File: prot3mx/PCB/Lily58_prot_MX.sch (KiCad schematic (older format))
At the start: 87 parts, among them J1 LED, J2 4PIN, J3 OLED, P1 i2c_pin, P2 i2c_pin, SW1 SW_PUSH, SW10 SW_PUSH, SW11 SW_PUSH, SW12 SW_PUSH, SW13 SW_PUSH, SW14 SW_PUSH, SW15 SW_PUSH, SW16 SW_PUSH, SW17 SW_PUSH, SW18 SW_PUSH, SW19 SW_PUSH, SW2 SW_PUSH, SW20 SW_PUSH, SW21 SW_PUSH, SW22 SW_PUSH, SW23 SW_PUSH, SW24 SW_PUSH, SW25 SW_PUSH, SW26 SW_PUSH, SW27 SW_PUSH, SW28 SW_PUSH, SW29 SW_PUSH, SW3 SW_PUSH, SW30 ROT_ENC_SW, SW31 ROT_ENC_SW, SW32 ROT_ENC_SW, SW4 SW_PUSH, SW5 SW_PUSH, SW6 SW_PUSH, SW7 SW_PUSH, SW8 SW_PUSH, SW9 SW_PUSH, U1 ProMicro

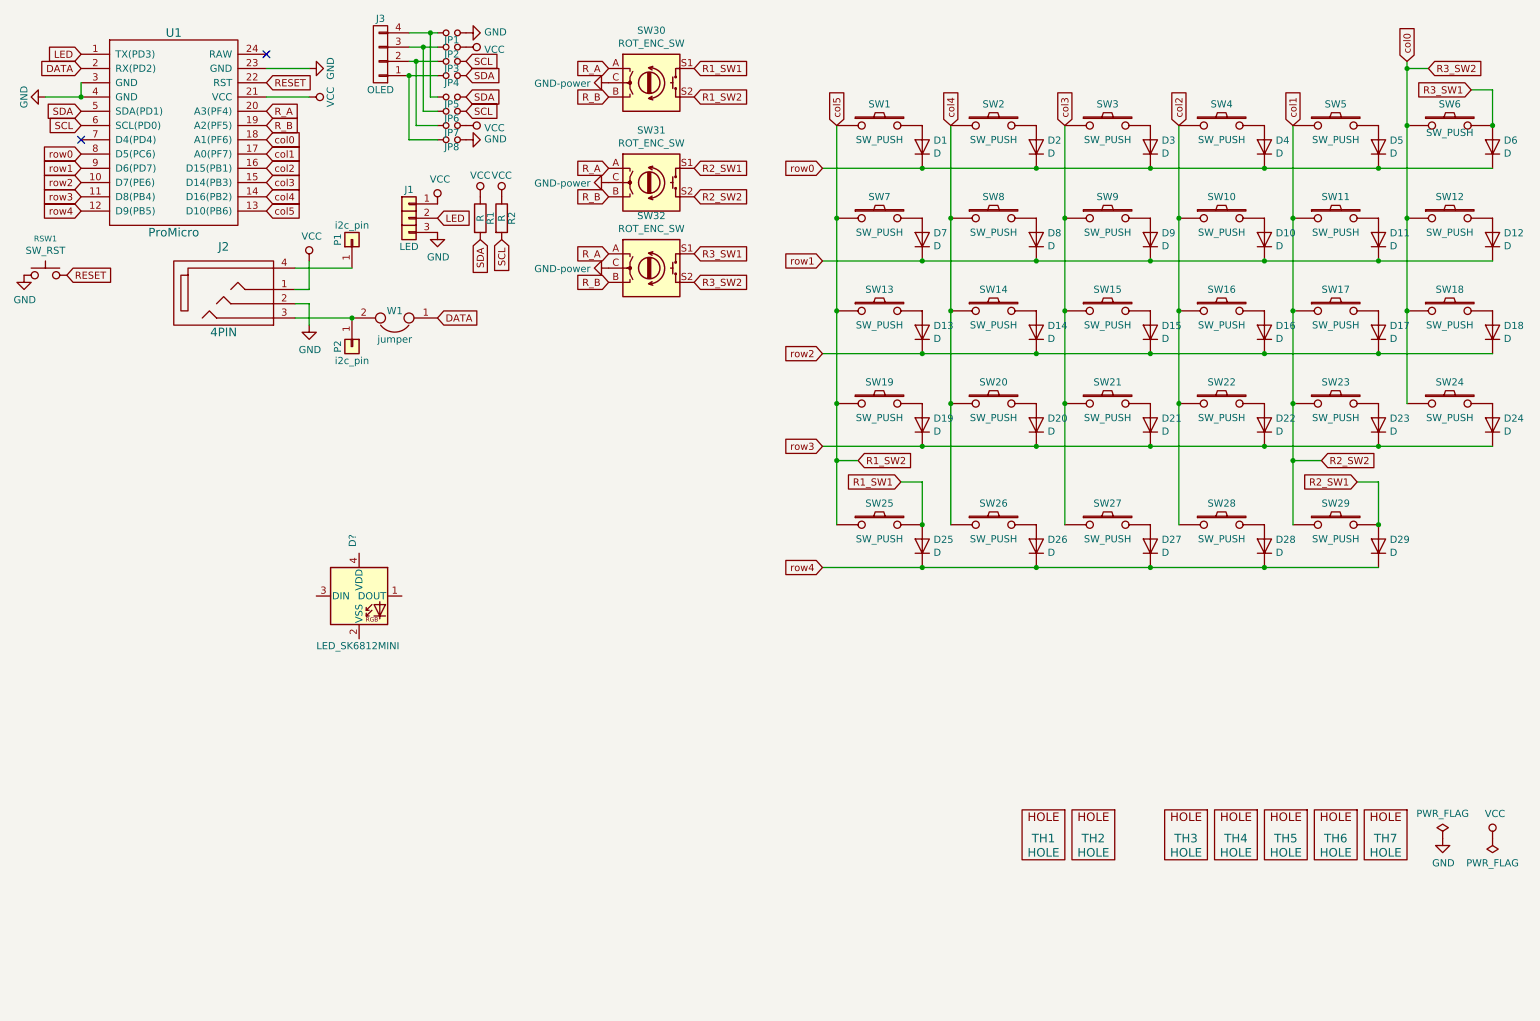
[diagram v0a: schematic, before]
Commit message: LEDs added to schematic; switch footprints flippped; tracks deleted; rerouting started
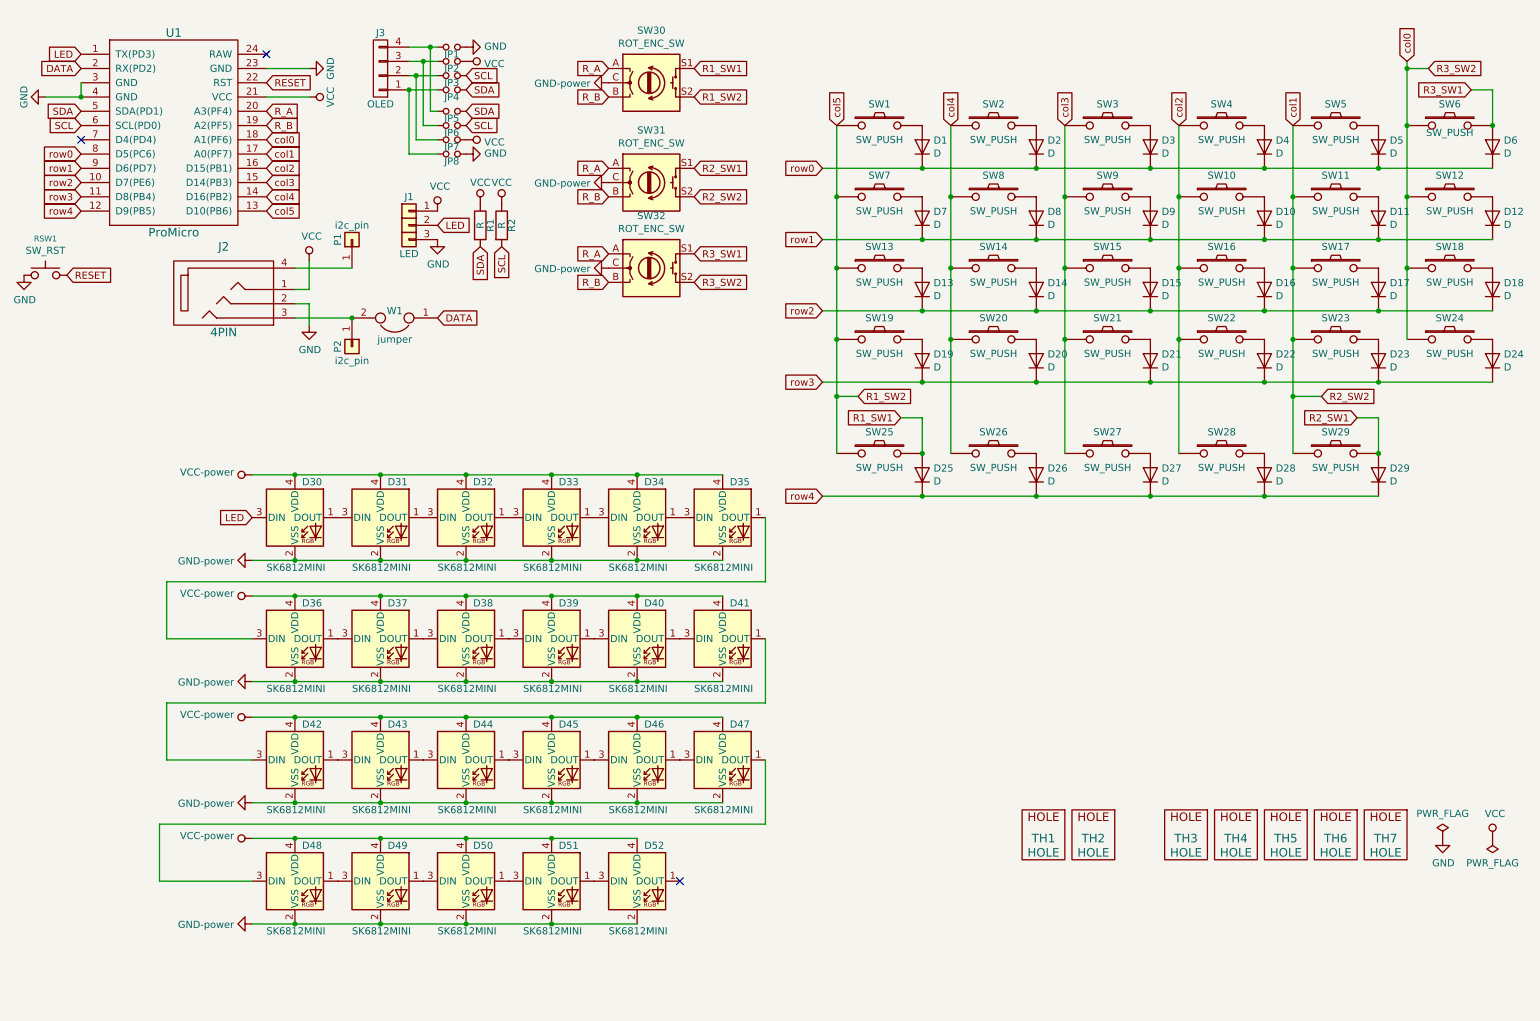
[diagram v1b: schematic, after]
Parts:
- added D31, D32, D33, D34, D35, D36, D37, D38, D39, D40, D41, D42, D43, D44, D45, D46, D47, D48, D49, D50, D51, D52: SK6812MINI, Lily58_prot_MX-footprint:SK6812MINI_rev, symbol Lily58_prot_MX-rescue:LED_SK6812MINI
- D30: renamed from D?; value LED_SK6812MINI -> SK6812MINI; footprint LED_SMD:LED_SK6812MINI_PLCC4_3.5x3.5mm_P1.75mm -> Lily58_prot_MX-footprint:SK6812MINI_rev
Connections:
- net GND: now also D30.2 (VSS), D31.2 (VSS), D32.2 (VSS), D33.2 (VSS), D34.2 (VSS), D35.2 (VSS), D36.2 (VSS), D37.2 (VSS), D38.2 (VSS), D39.2 (VSS), D40.2 (VSS), D41.2 (VSS), D42.2 (VSS), D43.2 (VSS), D44.2 (VSS), D45.2 (VSS), D46.2 (VSS), D47.2 (VSS), D48.2 (VSS), D49.2 (VSS), D50.2 (VSS), D51.2 (VSS), D52.2 (VSS)
- net LED: now also D30.3 (DIN)
- net VCC: now also D30.4 (VDD), D31.4 (VDD), D32.4 (VDD), D33.4 (VDD), D34.4 (VDD), D35.4 (VDD), D36.4 (VDD), D37.4 (VDD), D38.4 (VDD), D39.4 (VDD), D40.4 (VDD), D41.4 (VDD), D42.4 (VDD), D43.4 (VDD), D44.4 (VDD), D45.4 (VDD), D46.4 (VDD), D47.4 (VDD), D48.4 (VDD), D49.4 (VDD), D50.4 (VDD), D51.4 (VDD), D52.4 (VDD)
- net at D30.1 (DOUT): now also D31.3 (DIN)
- new net: D31.1 (DOUT), D32.3 (DIN)
- new net: D32.1 (DOUT), D33.3 (DIN)
- new net: D33.1 (DOUT), D34.3 (DIN)
- new net: D34.1 (DOUT), D35.3 (DIN)
- new net: D35.1 (DOUT), D36.3 (DIN)
- new net: D36.1 (DOUT), D37.3 (DIN)
- new net: D37.1 (DOUT), D38.3 (DIN)
- new net: D38.1 (DOUT), D39.3 (DIN)
- new net: D39.1 (DOUT), D40.3 (DIN)
- new net: D40.1 (DOUT), D41.3 (DIN)
- new net: D41.1 (DOUT), D42.3 (DIN)
- new net: D42.1 (DOUT), D43.3 (DIN)
- new net: D43.1 (DOUT), D44.3 (DIN)
- new net: D44.1 (DOUT), D45.3 (DIN)
- new net: D45.1 (DOUT), D46.3 (DIN)
- new net: D46.1 (DOUT), D47.3 (DIN)
- new net: D47.1 (DOUT), D48.3 (DIN)
- new net: D48.1 (DOUT), D49.3 (DIN)
- new net: D49.1 (DOUT), D50.3 (DIN)
- new net: D50.1 (DOUT), D51.3 (DIN)
- new net: D51.1 (DOUT), D52.3 (DIN)
- no-connect marks 2 -> 3
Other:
- moved on the sheet: D10, D11, D12, D13, D14, D15, D16, D17, D18, D19, D20, D21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

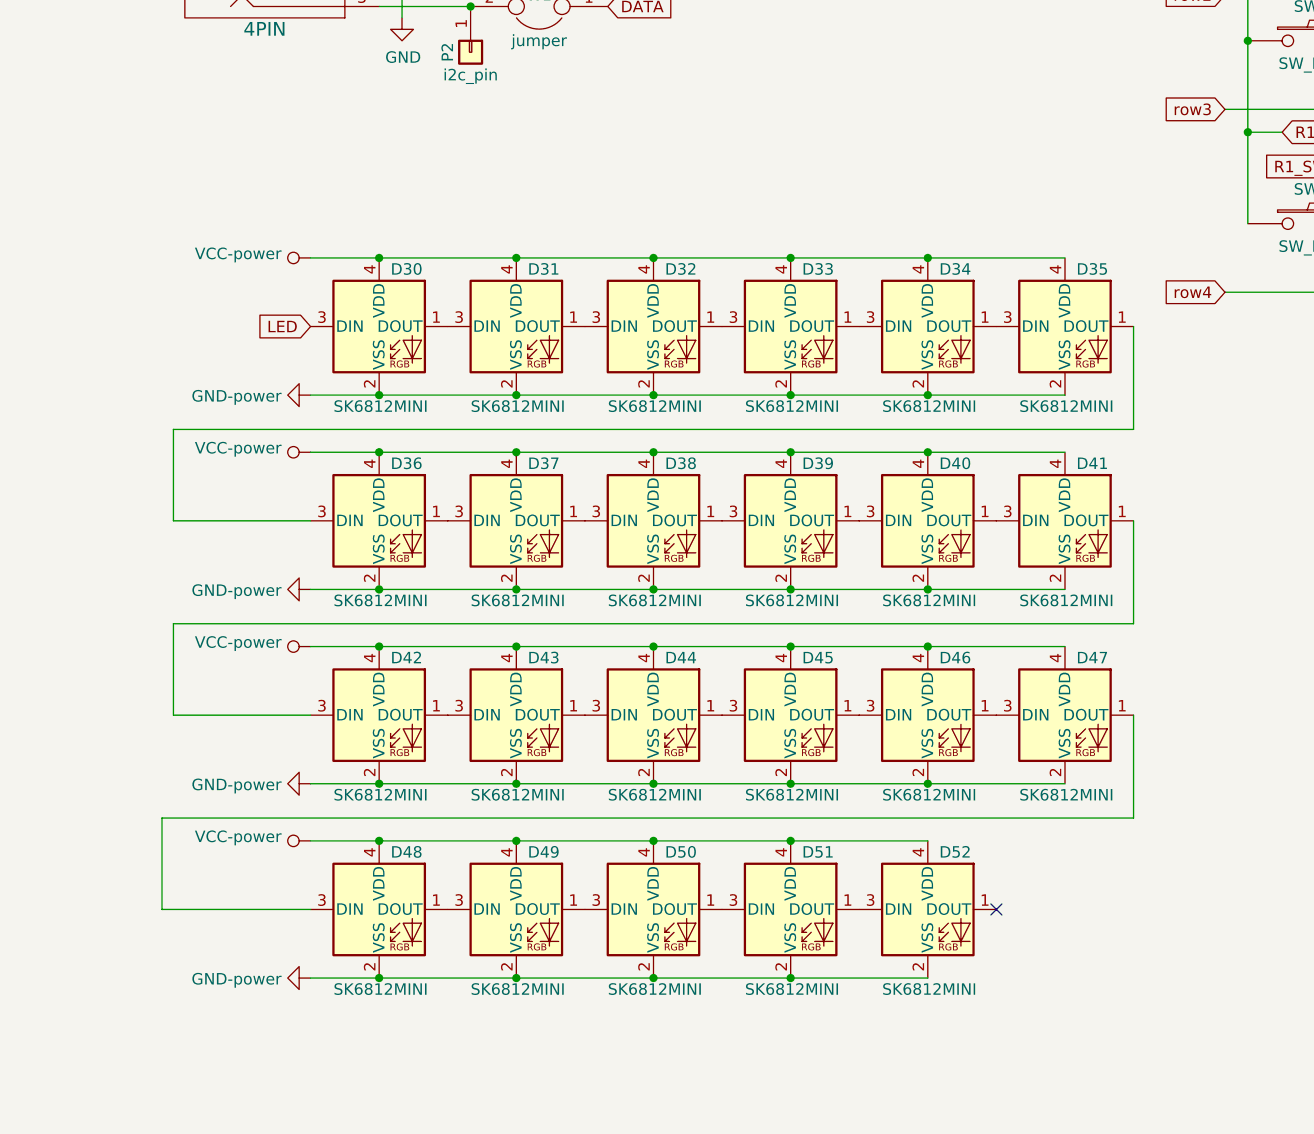
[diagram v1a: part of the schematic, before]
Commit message: modified SK6812 footprint to include cutout
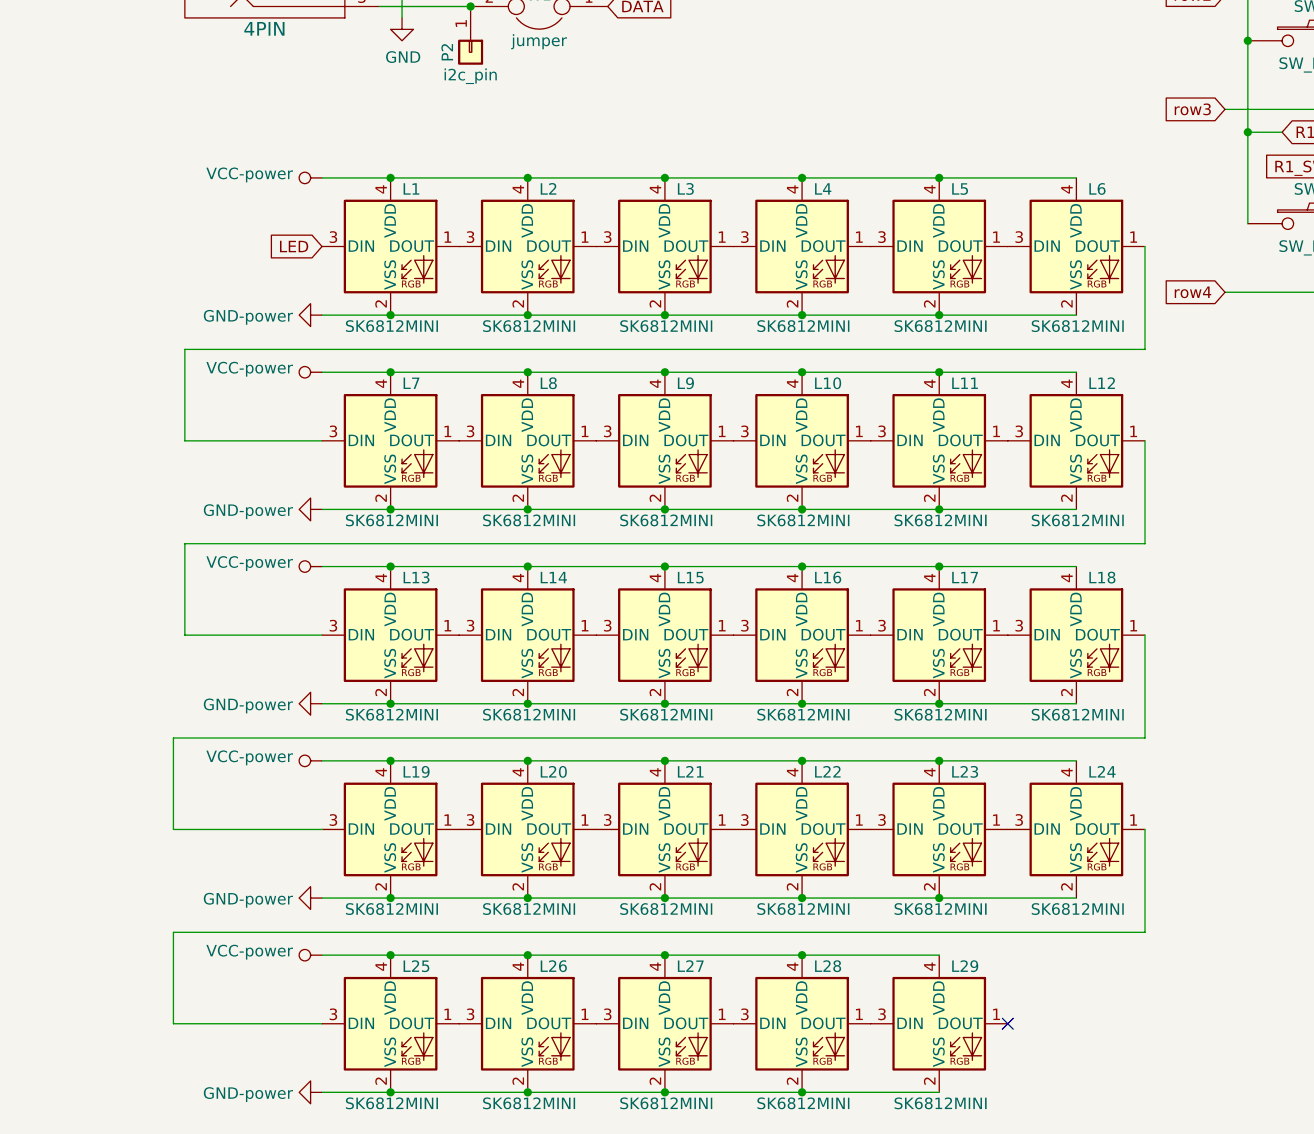
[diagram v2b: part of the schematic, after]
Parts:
- removed D31, D32, D33, D34, D35, D36, D37, D38, D39, D40, D41, D42, D43, D44, D45, D46, D47, D48, D49, D50, D51, D52: SK6812MINI, Lily58_prot_MX-footprint:SK6812MINI_rev, symbol Lily58_prot_MX-rescue:LED_SK6812MINI
- added L10, L11, L12, L13, L14, L15, L16, L17, L18, L19, L2, L20, L21, L22, L23, L24, L25, L26, L27, L28, L29, L3, L4, L5, L6, L7, L8, L9: SK6812MINI, Lily58_prot_MX-footprint:SK6812MINI_rev_w_co, symbol Lily58_prot_MX-rescue:LED_SK6812MINI
- L1: renamed from D30; footprint Lily58_prot_MX-footprint:SK6812MINI_rev -> Lily58_prot_MX-footprint:SK6812MINI_rev_w_co
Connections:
- net GND: now also L10.2 (VSS), L11.2 (VSS), L12.2 (VSS), L13.2 (VSS), L14.2 (VSS), L15.2 (VSS), L16.2 (VSS), L17.2 (VSS), L18.2 (VSS), L19.2 (VSS), L2.2 (VSS), L20.2 (VSS), L21.2 (VSS), L22.2 (VSS), L23.2 (VSS), L24.2 (VSS), L25.2 (VSS), L26.2 (VSS), L27.2 (VSS), L28.2 (VSS), L29.2 (VSS), L3.2 (VSS), L4.2 (VSS), L5.2 (VSS), L6.2 (VSS), L7.2 (VSS), L8.2 (VSS), L9.2 (VSS)
- net VCC: now also L10.4 (VDD), L11.4 (VDD), L12.4 (VDD), L13.4 (VDD), L14.4 (VDD), L15.4 (VDD), L16.4 (VDD), L17.4 (VDD), L18.4 (VDD), L19.4 (VDD), L2.4 (VDD), L20.4 (VDD), L21.4 (VDD), L22.4 (VDD), L23.4 (VDD), L24.4 (VDD), L25.4 (VDD), L26.4 (VDD), L27.4 (VDD), L28.4 (VDD), L29.4 (VDD), L3.4 (VDD), L4.4 (VDD), L5.4 (VDD), L6.4 (VDD), L7.4 (VDD), L8.4 (VDD), L9.4 (VDD)
- net at L1.1 (DOUT): now also L2.3 (DIN)
- new net: L2.1 (DOUT), L3.3 (DIN)
- new net: L3.1 (DOUT), L4.3 (DIN)
- new net: L4.1 (DOUT), L5.3 (DIN)
- new net: L5.1 (DOUT), L6.3 (DIN)
- new net: L6.1 (DOUT), L7.3 (DIN)
- new net: L7.1 (DOUT), L8.3 (DIN)
- new net: L8.1 (DOUT), L9.3 (DIN)
- new net: L10.3 (DIN), L9.1 (DOUT)
- new net: L10.1 (DOUT), L11.3 (DIN)
- new net: L11.1 (DOUT), L12.3 (DIN)
- new net: L12.1 (DOUT), L13.3 (DIN)
- new net: L13.1 (DOUT), L14.3 (DIN)
- new net: L14.1 (DOUT), L15.3 (DIN)
- new net: L15.1 (DOUT), L16.3 (DIN)
- new net: L16.1 (DOUT), L17.3 (DIN)
- new net: L17.1 (DOUT), L18.3 (DIN)
- new net: L18.1 (DOUT), L19.3 (DIN)
- new net: L19.1 (DOUT), L20.3 (DIN)
- new net: L20.1 (DOUT), L21.3 (DIN)
- new net: L21.1 (DOUT), L22.3 (DIN)
- new net: L22.1 (DOUT), L23.3 (DIN)
- new net: L23.1 (DOUT), L24.3 (DIN)
- new net: L24.1 (DOUT), L25.3 (DIN)
- new net: L25.1 (DOUT), L26.3 (DIN)
- new net: L26.1 (DOUT), L27.3 (DIN)
- new net: L27.1 (DOUT), L28.3 (DIN)
- new net: L28.1 (DOUT), L29.3 (DIN)
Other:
- moved on the sheet: L1
